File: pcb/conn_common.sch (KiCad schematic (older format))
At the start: 7 parts

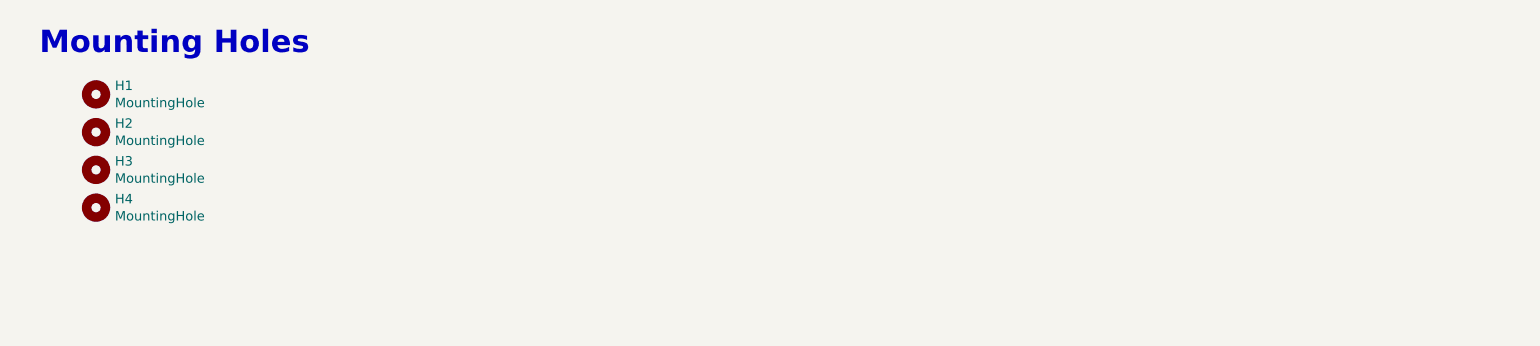
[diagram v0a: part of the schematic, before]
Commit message: pcb: cleanup power handle silkscreen, edge cuts
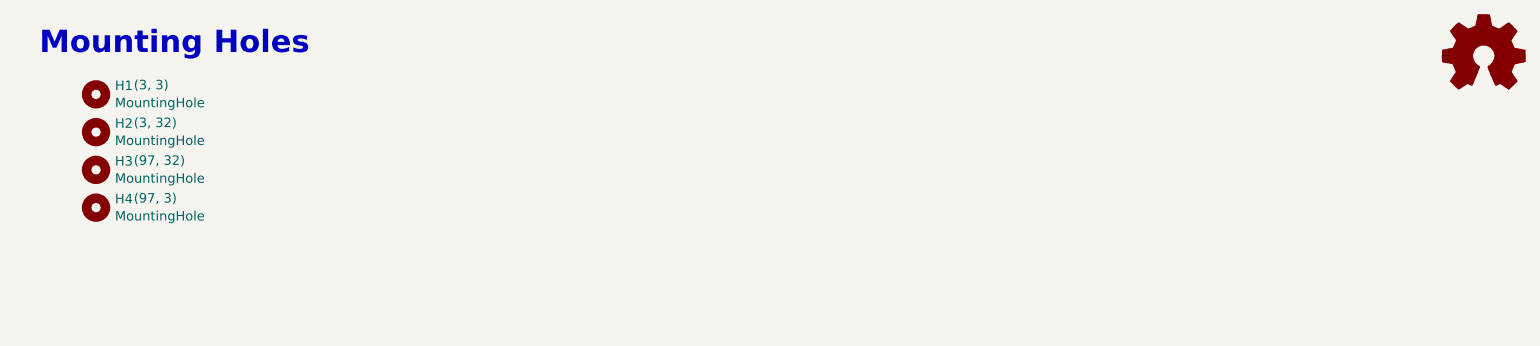
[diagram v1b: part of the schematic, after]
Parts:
- added LOGO1: Logo_Open_Hardware_Small, Symbol:OSHW-Logo_5.7x6mm_SilkScreen, symbol Graphic:Logo_Open_Hardware_Small
- H1: Location (none) -> (3, 3)
- H2: Location (none) -> (3, 32)
- H3: Location (none) -> (97, 32)
- H4: Location (none) -> (97, 3)
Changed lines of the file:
@@
 F 2 "MountingHole:MountingHole_2.7mm_M2.5" H 3350 1150 50  0001 C CNN
 F 3 "~" H 3350 1150 50  0001 C CNN
+F 4 "(3, 3)" H 3550 1200 50  0000 L CNN "Location"
 	1    3350 1150
 	1    0    0    -1
@@
 F 2 "MountingHole:MountingHole_2.7mm_M2.5" H 3350 1350 50  0001 C CNN
 F 3 "~" H 3350 1350 50  0001 C CNN
+F 4 "(3, 32)" H 3550 1400 50  0000 L CNN "Location"
 	1    3350 1350
 	1    0    0    -1
@@
 F 2 "MountingHole:MountingHole_2.7mm_M2.5" H 3350 1550 50  0001 C CNN
 F 3 "~" H 3350 1550 50  0001 C CNN
+F 4 "(97, 32)" H 3550 1600 50  0000 L CNN "Location"
 	1    3350 1550
 	1    0    0    -1
@@
 F 2 "MountingHole:MountingHole_2.7mm_M2.5" H 3350 1750 50  0001 C CNN
 F 3 "~" H 3350 1750 50  0001 C CNN
+F 4 "(97, 3)" H 3550 1800 50  0000 L CNN "Location"
 	1    3350 1750
 	1    0    0    -1
 $EndComp
+$Comp
+L Graphic:Logo_Open_Hardware_Small LOGO1
+U 1 1 6195747A
+P 10700 950
+F 0 "LOGO1" H 10700 1225 50  0001 C CNN
+F 1 "Logo_Open_Hardware_Small" H 10700 725 50  0001 C CNN
+F 2 "Symbol:OSHW-Logo_5.7x6mm_SilkScreen" H 10700 950 50  0001 C CNN
+F 3 "~" H 10700 950 50  0001 C CNN
+	1    10700 950
+	1    0    0    -1
+$EndComp
